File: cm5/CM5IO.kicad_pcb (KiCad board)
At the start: 4 copper layers, 101.9 x 90.8 mm, 67 parts, among them J1 67910-5700, J14 JST_SHBM04B-SRSS-TB, J2 B2B-XH-A_LF__SN_, J4 0786463001, J5 USB3_A, J6 Conn_02x03_Counter_Clockwise, J7 Conn_01x04, U2 TLV320ADC6120IRTER, U5 74LVC1G07SE-7, U6 AP22653W6, U8 AP3441SHE-7B

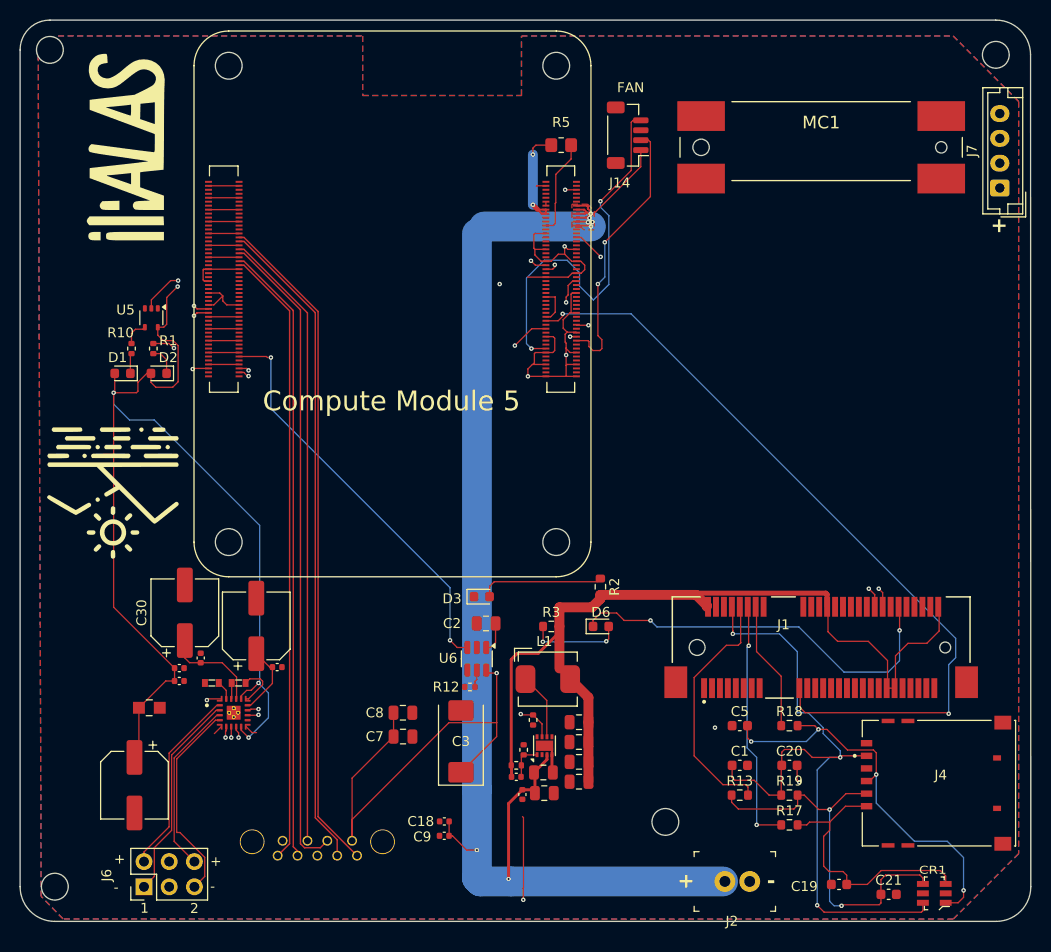
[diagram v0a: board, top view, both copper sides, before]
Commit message: Ordered v2 PCB
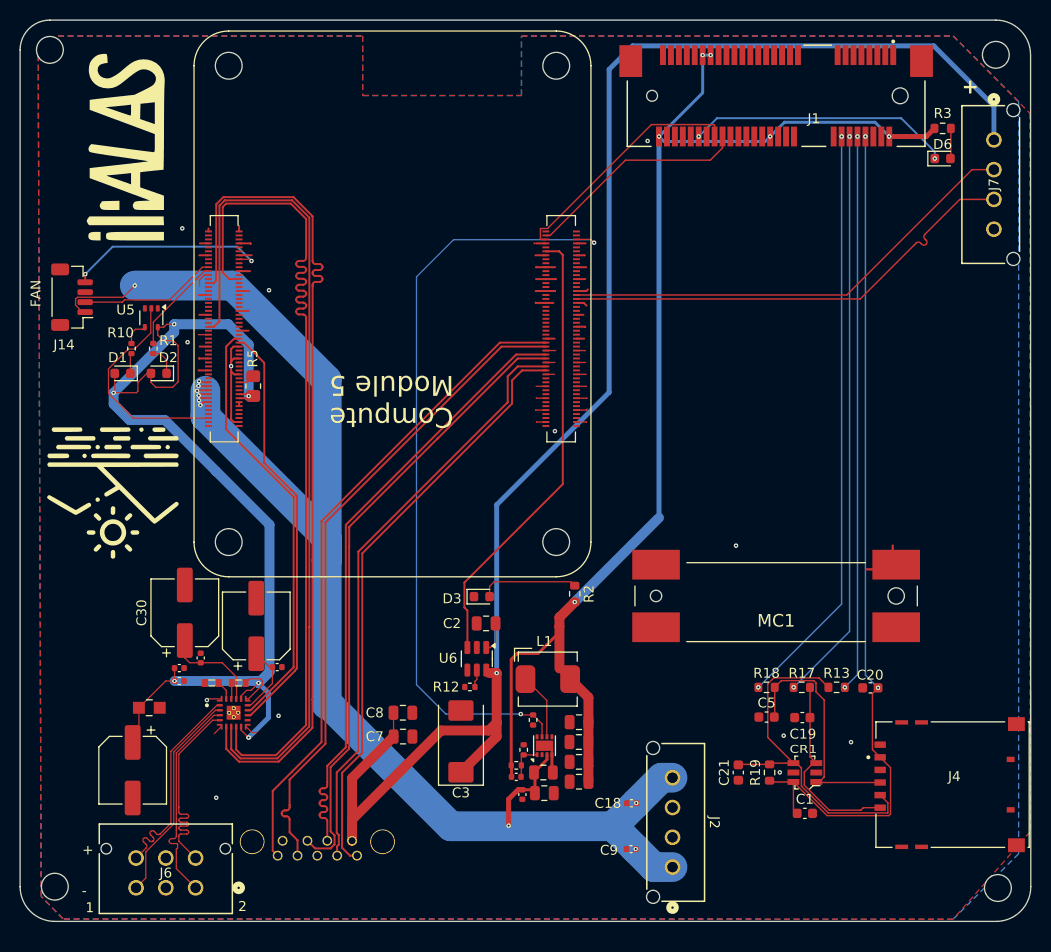
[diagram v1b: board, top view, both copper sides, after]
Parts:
- J2: value B2B-XH-A_LF__SN_ -> 1x4; footprint digikey-footprints:PinHeader_1x2_P2.5mm_Drill1.1mm -> Connector_Molex:CONN_SD-43650-006_04_MOL 1x4
- J6: footprint Connector_PinHeader_2.54mm:PinHeader_2x03_P2.54mm_Vertical -> Connector_Molex:CONN_SD-43045-005_06_MOL 2x3
- J7: footprint Connector_JST:JST_EH_B4B-EH-A_1x04_P2.50mm_Vertical -> Connector_Molex:CONN_SD-43650-006_04_MOL 1x4
- moved R3 63.8 mm to (234.4, 79.8), turned to 180 degrees
- moved D6 58.4 mm to (234.4, 82.9)
- moved J14 58.3 mm to (146.7, 96.8)
- moved Module1 58.2 mm to (162.5, 121.5), turned to 0 degrees
- moved J1 55.8 mm to (217.7, 76.5), turned to 180 degrees
- moved MC1 45.4 mm to (217.7, 126.9), turned to 180 degrees
- moved R5 39.4 mm to (165.0, 105.8), turned to 90 degrees
- moved H8 34.2 mm to (240.0, 156.4)
- moved C21 19.5 mm to (213.8, 144.7), turned to -90 degrees
- moved C18 18.9 mm to (203.1, 147.8)
- moved C9 18.9 mm to (203.0, 152.4)
- moved CR1 17.8 mm to (220.6, 144.7)
- moved C19 17.2 mm to (220.3, 139.2)
- moved R13 14.6 mm to (223.8, 136.1)
- moved R17 13.9 mm to (220.3, 136.1)
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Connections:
- J1 pad 17: /CM5_GPIO ( Ethernet, GPIO, SDCARD)/GPIO6 -> /PCIe-M2/RI
- J2 pad 1: GND -> /+5v
- J2 pad 2: /+5v -> GND
- J6 pad 2: Net-(J6-Pin_2) -> GND
- J6 pad 3: GND -> Net-(J6-Pin_3)
- J6 pad 4: GND -> Net-(J6-Pin_4)
- J6 pad 5: Net-(J6-Pin_5) -> GND
- U2 pad 1: Net-(J6-Pin_2) -> Net-(J6-Pin_6)
- U2 pad 2: Net-(J6-Pin_1) -> Net-(J6-Pin_3)
- U2 pad 3: Net-(J6-Pin_6) -> Net-(J6-Pin_1)
- U2 pad 4: Net-(J6-Pin_5) -> Net-(J6-Pin_4)
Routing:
- net /CM5_GPIO ( Ethernet, GPIO, SDCARD)/GPIO6: track 80.3 -> 0.00 mm, vias 2 -> 0
- net /CM5_HighSpeed/USB2_N: track 74.6 -> 22.6 mm, vias 2 -> 0
- net /CM5_HighSpeed/USB2_P: track 75.7 -> 24.7 mm, vias 2 -> 0
- net /+3.3v: track 161.7 -> 113.1 mm
- net /CM5_HighSpeed/USB3-0-D_P: track 95.4 -> 47.3 mm, vias 1 -> 0
- net /PCIe-M2/SIM_RST: track 13.0 -> 59.0 mm, vias 0 -> 2
- net GND: track 126.1 -> 80.5 mm, vias 9 -> 13
- net /CM5_HighSpeed/USB3-0-D_N: track 92.6 -> 47.3 mm, vias 1 -> 0
- net /CM5_GPIO ( Ethernet, GPIO, SDCARD)/GPIO2: track 85.3 -> 42.5 mm, vias 2 -> 0
- net /CM5_HighSpeed/VBUS: track 119.0 -> 159.2 mm
- net /CM5_GPIO ( Ethernet, GPIO, SDCARD)/GPIO3: track 80.6 -> 43.2 mm, vias 2 -> 0
- net /PCIe-M2/M2_3v3: track 96.3 -> 132.1 mm, vias 0 -> 6
- net Net-(Module1A-LED_nACT): track 43.3 -> 9.85 mm, vias 2 -> 0
- net /PCIe-M2/SIM_CLK: track 24.9 -> 57.8 mm
- net /PCIe-M2/SIM_DATA: track 25.2 -> 56.0 mm, vias 0 -> 2
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- removed copper zone on F.Cu, net /+5v

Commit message: Oops, basically brand new ADC design using a new chip
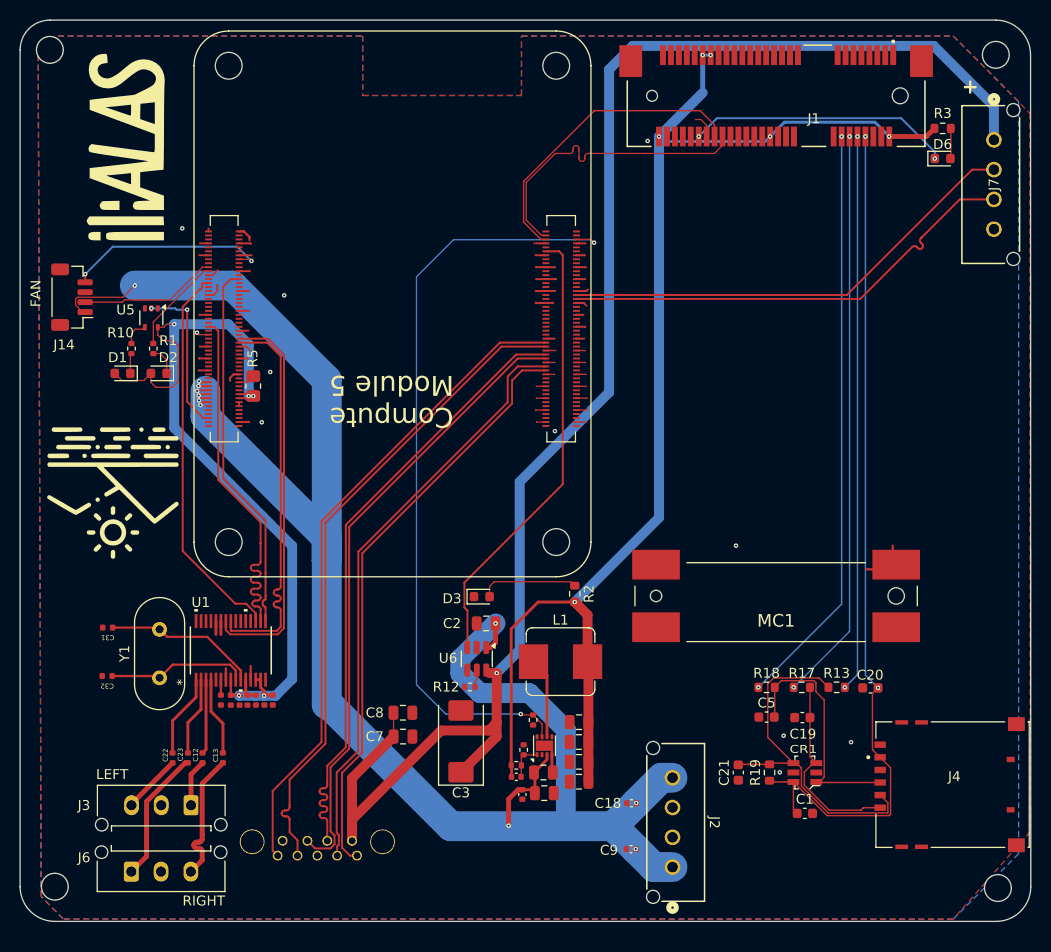
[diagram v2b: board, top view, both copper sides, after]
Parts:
- removed U2: TLV320ADC6120IRTER, TLV320ADC6120IRTER:IC_TLV320ADC6120IRTER
- added C22: 10uF, PCM_JLCPCB:C_0402, F.Cu at (156.8, 143.2)
- added C23: 10uF, PCM_JLCPCB:C_0402, F.Cu at (158.4, 143.2)
- added C32: 15pF, PCM_JLCPCB:C_0402, F.Cu at (150.2, 135.0)
- added J3: Conn_01x03, Connector_Molex:Molex_Micro-Fit_3.0_43650-0315_1x03_P3.00mm_Vertical, F.Cu at (158.7, 148.0)
- added U1: PCM1863DBT, PCM:DBT30_TEX, F.Cu at (162.7, 132.4)
- added Y1: Crystal (24.576MHz), Crystal:Crystal_HC49-U_Vertical, F.Cu at (155.5, 135.2)
- C12, C13: value 1uF -> 10uF; footprint digikey-footprints:0603 -> PCM_JLCPCB:C_0402
- C24: footprint digikey-footprints:0805 -> PCM_JLCPCB:C_0402
- C25, C29: value 100n -> 10uF; footprint Capacitor_SMD:C_0402_1005Metric -> PCM_JLCPCB:C_0402
- C26: value 100n -> 100nF; footprint Capacitor_SMD:C_0402_1005Metric -> PCM_JLCPCB:C_0402
- C27: footprint Capacitor_SMD:CP_Elec_6.3x5.9 -> PCM_JLCPCB:C_0402
- C28, C30: value 10uF -> 100nF; footprint Capacitor_SMD:CP_Elec_6.3x5.9 -> PCM_JLCPCB:C_0402
- C31: value 100n -> 15pF; footprint Capacitor_SMD:C_0402_1005Metric -> PCM_JLCPCB:C_0402
- J6: value Conn_02x03_Counter_Clockwise -> Conn_01x03; footprint Connector_Molex:CONN_SD-43045-005_06_MOL 2x3 -> Connector_Molex:Molex_Micro-Fit_3.0_43650-0315_1x03_P3.00mm_Vertical
- L1: footprint CM5IO:L_Bourns_SRP5030CC -> Inductor_SMD:L_Bourns_SRP7028A_7.3x6.6mm
- moved C27 15.8 mm to (166.9, 137.4), turned to 90 degrees
- moved C30 11.3 mm to (165.2, 137.4), turned to -90 degrees
- moved C31 9.86 mm to (150.3, 130.1), turned to 180 degrees
- moved C13 7.71 mm to (161.9, 143.2), turned to 90 degrees
- moved C12 7.61 mm to (159.9, 143.2), turned to 90 degrees
- moved C28 7.51 mm to (166.1, 137.4), turned to -90 degrees
- moved C24 7.25 mm to (161.7, 137.4), turned to 90 degrees
- moved J6 6.68 mm to (152.7, 154.7)
- moved C25 6.37 mm to (163.6, 137.4), turned to 90 degrees
- moved C26 6.11 mm to (162.7, 137.4), turned to 90 degrees
- moved C29 4.48 mm to (164.4, 137.4), turned to 90 degrees
- moved L1 2.18 mm to (195.9, 133.6)
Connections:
- net /PCIe-M2/DTR renamed /Cellular/DTR
- net /PCIe-M2/FB renamed /Cellular/FB
- net /PCIe-M2/LED_WWAN renamed /Cellular/LED_WWAN
- net /PCIe-M2/M2_3v3 renamed /Cellular/M2_3v3
- net /PCIe-M2/PERST renamed /Cellular/PERST
- net /PCIe-M2/RI renamed /Cellular/RI
- net /PCIe-M2/SIM_CLK renamed /Cellular/SIM_CLK
- net /PCIe-M2/SIM_DATA renamed /Cellular/SIM_DATA
- net /PCIe-M2/SIM_RST renamed /Cellular/SIM_RST
- net /PCIe-M2/SIM_VDD renamed /Cellular/SIM_VDD
- net /PCIe-M2/W_DISABLE renamed /Cellular/W_DISABLE
- C12 pad 1: Net-(U2-MICBIAS_GPI2) -> /CM5_GPIO ( Ethernet, GPIO, SDCARD)/Audio/LP
- C12 pad 2: GND -> /CM5_GPIO ( Ethernet, GPIO, SDCARD)/Audio/VIN1P
- C13 pad 1: Net-(U2-VREF) -> /CM5_GPIO ( Ethernet, GPIO, SDCARD)/Audio/RP
- C13 pad 2: GND -> /CM5_GPIO ( Ethernet, GPIO, SDCARD)/Audio/VIN2P
- C2 pad 1: /CM5_HighSpeed/+5v -> /+5v
- C24 pad 1: /+3.3v -> GND
- C24 pad 2: GND -> Net-(U1-VREF)
- C25 pad 1: /+3.3v -> GND
- C25 pad 2: GND -> /+3.3v
- C26 pad 1: /+3.3v -> GND
- C26 pad 2: GND -> /+3.3v
- C27 pad 1: /+3.3v -> GND
- C27 pad 2: GND -> /+3.3v
- C28 pad 1: /CM5_GPIO ( Ethernet, GPIO, SDCARD)/DREG -> /+3.3v
- C29 pad 1: /CM5_GPIO ( Ethernet, GPIO, SDCARD)/DREG -> GND
- C29 pad 2: GND -> /CM5_GPIO ( Ethernet, GPIO, SDCARD)/Audio/LDO
- C30 pad 1: /CM5_GPIO ( Ethernet, GPIO, SDCARD)/AREG -> /CM5_GPIO ( Ethernet, GPIO, SDCARD)/Audio/LDO
- C31 pad 1: /CM5_GPIO ( Ethernet, GPIO, SDCARD)/AREG -> /CM5_GPIO ( Ethernet, GPIO, SDCARD)/Audio/XI
- J6 pad 1: Net-(J6-Pin_1) -> /CM5_GPIO ( Ethernet, GPIO, SDCARD)/Audio/RN
- J6 pad 3: Net-(J6-Pin_3) -> /CM5_GPIO ( Ethernet, GPIO, SDCARD)/Audio/RP
- Module1 pad 89: /CM5_GPIO ( Ethernet, GPIO, SDCARD)/WL_nDis -> unconnected-(Module1A-WiFi_nDisable-Pad89)
- Module1 pad 91: /CM5_GPIO ( Ethernet, GPIO, SDCARD)/BT_nDis -> unconnected-(Module1A-BT_nDisable-Pad91)
- Module1 pad 97: /CM5_GPIO ( Ethernet, GPIO, SDCARD)/CAM_GPIO0 -> unconnected-(Module1A-CAM_GPIO0-Pad97)
- U6 pad 1: /CM5_HighSpeed/+5v -> /+5v
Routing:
- net /CM5_GPIO ( Ethernet, GPIO, SDCARD)/GPIO19: track 86.7 -> 37.7 mm
- net /CM5_GPIO ( Ethernet, GPIO, SDCARD)/GPIO18: track 86.1 -> 37.5 mm
- net /CM5_GPIO ( Ethernet, GPIO, SDCARD)/GPIO20: track 86.7 -> 39.1 mm
- net /+5v: track 152.8 -> 185.1 mm, vias 10 -> 11
- net /+3.3v: track 113.1 -> 86.0 mm, vias 6 -> 5
- net Net-(J6-Pin_3): track 21.6 -> 0.00 mm
- net Net-(J6-Pin_1): track 21.6 -> 0.00 mm
- net Net-(J6-Pin_6): track 21.6 -> 0.00 mm
- net Net-(J6-Pin_4): track 21.5 -> 0.00 mm
- net /CM5_GPIO ( Ethernet, GPIO, SDCARD)/Audio/XI: track 0.00 -> 15.6 mm
- net /CM5_GPIO ( Ethernet, GPIO, SDCARD)/Audio/XO: track 0.00 -> 14.3 mm
- net /CM5_GPIO ( Ethernet, GPIO, SDCARD)/Audio/RN: track 0.00 -> 13.5 mm
- net /CM5_GPIO ( Ethernet, GPIO, SDCARD)/Audio/RP: track 0.00 -> 13.4 mm
- net /CM5_GPIO ( Ethernet, GPIO, SDCARD)/AREG: track 9.92 -> 0.00 mm
- net /CM5_HighSpeed/USB2_N: track 22.6 -> 31.0 mm
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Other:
- board text added: "LEFT"
- board text added: "RIGHT"
- board text removed: "-"
- board text removed: "1"
- board text removed: "2"

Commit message: Working PCB and working driver, sort of
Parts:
- Y1: footprint Crystal:Crystal_HC49-U_Vertical -> Crystal:S47SMD
- moved Y1 3.41 mm to (155.5, 131.8)
- moved C31 1.02 mm to (150.4, 129.1)
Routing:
- net /CM5_GPIO ( Ethernet, GPIO, SDCARD)/Audio/LP: track 4.90 -> 6.71 mm
- net /CM5_GPIO ( Ethernet, GPIO, SDCARD)/Audio/XO: track 14.3 -> 15.8 mm
- net GND: track 74.1 -> 75.3 mm, vias 13 -> 11
- net /CM5_GPIO ( Ethernet, GPIO, SDCARD)/Audio/LN: track 6.01 -> 6.83 mm
- net /CM5_GPIO ( Ethernet, GPIO, SDCARD)/Audio/VIN1P: track 7.52 -> 8.32 mm

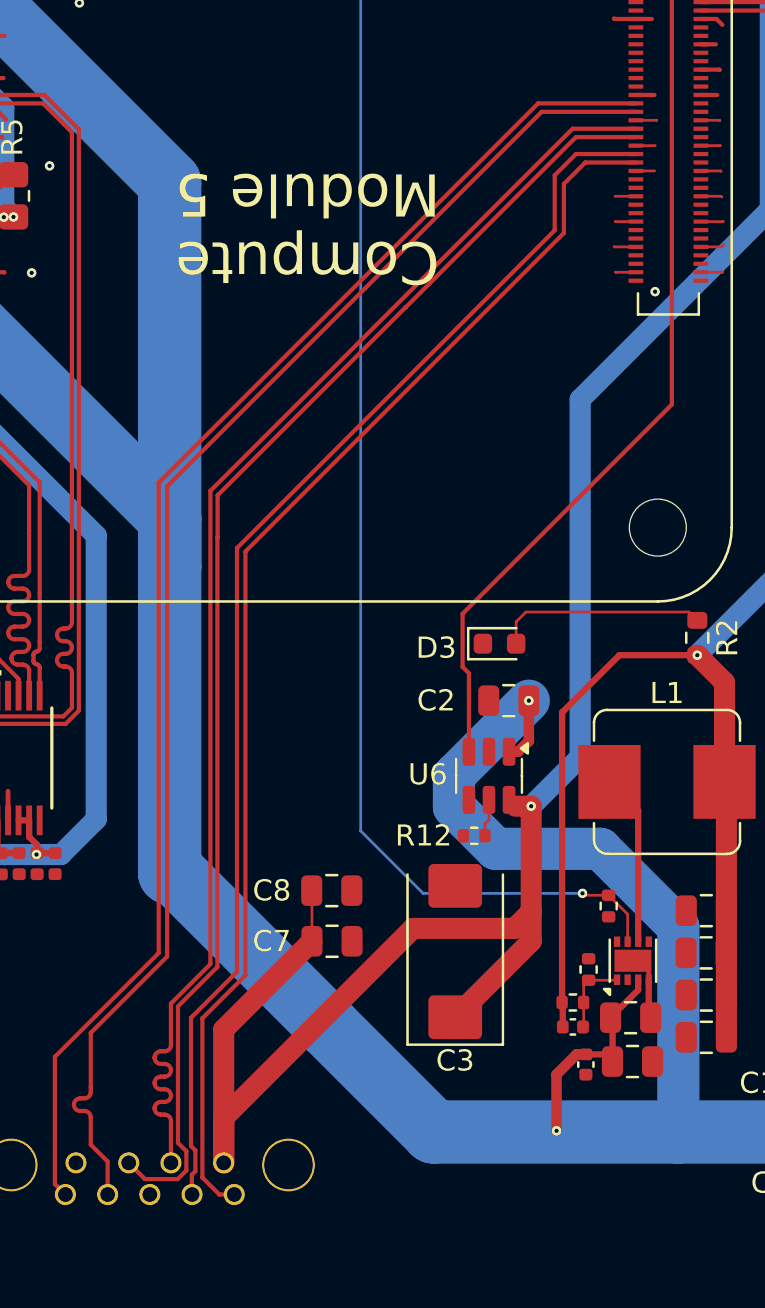
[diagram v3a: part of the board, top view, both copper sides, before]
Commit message: Fix the usb port (just in case) #1
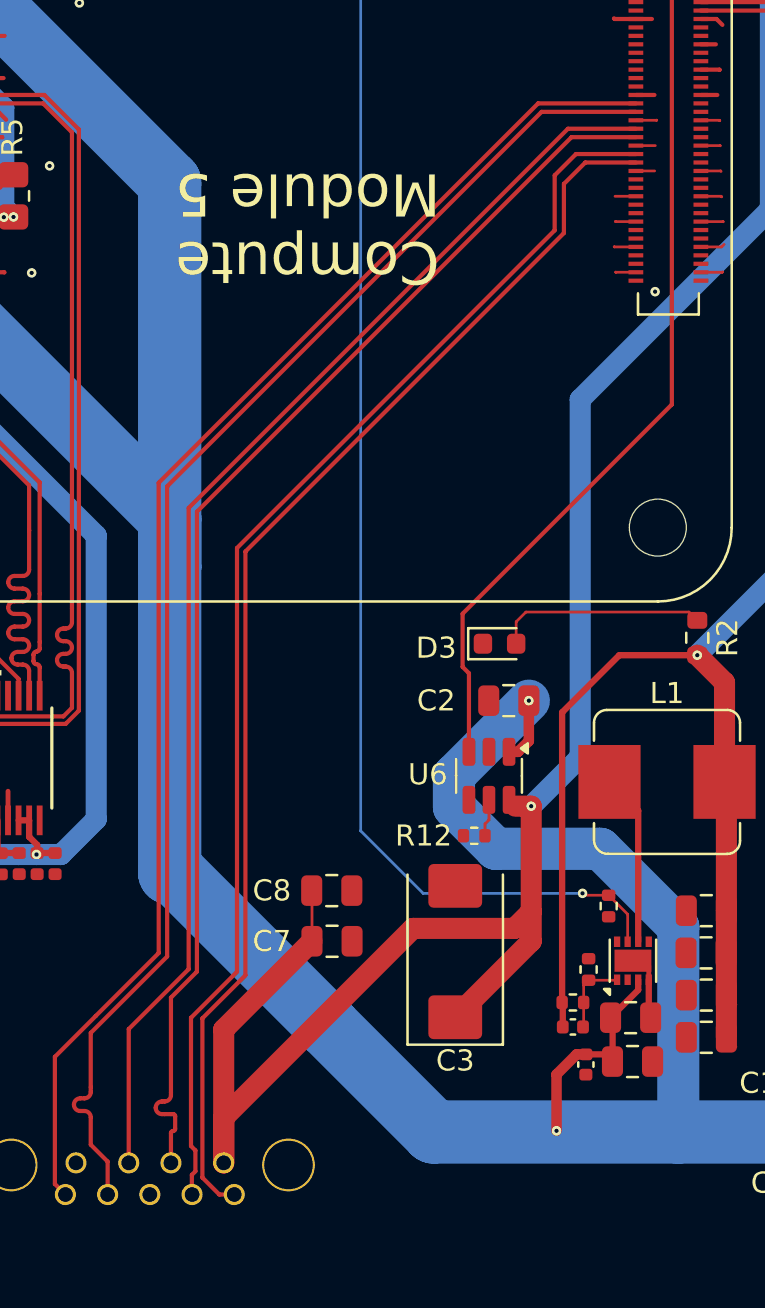
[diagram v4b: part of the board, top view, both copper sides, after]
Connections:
- J5 pad 2: /CM5_HighSpeed/USB3-1-D_P -> /CM5_HighSpeed/USB3-1-D_N
- J5 pad 3: /CM5_HighSpeed/USB3-1-D_N -> /CM5_HighSpeed/USB3-1-D_P
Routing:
- net /CM5_HighSpeed/USB3-1-D_N: track 63.0 -> 60.8 mm
- net /CM5_HighSpeed/USB3-1-D_P: track 62.9 -> 60.8 mm

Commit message: Getting started on StudioHub adapter
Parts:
- removed J5: USB3_A, Connector_USB:C168717
- added REF**: RJ45_Amphenol_54602-x08_Horizontal, Connector_RJ:RJ45_Amphenol_54602-x08_Horizontal, F.Cu at (167.8, 145.0)
- moved C7 2.56 mm to (181.1, 138.8)
- moved C8 2.56 mm to (181.1, 136.3)
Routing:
- net /CM5_HighSpeed/USB3-1-RX_N: track 66.0 -> 0.00 mm
- net /CM5_HighSpeed/USB3-1-RX_P: track 66.0 -> 0.00 mm
- net /CM5_HighSpeed/USB3-1-D_P: track 60.8 -> 0.00 mm
- net /CM5_HighSpeed/USB3-1-D_N: track 60.8 -> 0.00 mm
- net /CM5_HighSpeed/USB3-1-TX_N: track 59.9 -> 0.00 mm
- net /CM5_HighSpeed/USB3-1-TX_P: track 59.9 -> 0.00 mm
- net /CM5_HighSpeed/VBUS: track 159.2 -> 135.2 mm
